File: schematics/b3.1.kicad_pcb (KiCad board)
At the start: 2 copper layers, 69.5 x 25 mm, 48 parts, among them J1 PowerInput, J2 PowerPassThru, J3 OutputPins, U1 INA128, U2 INA128, U3 INA128, U4 INA128

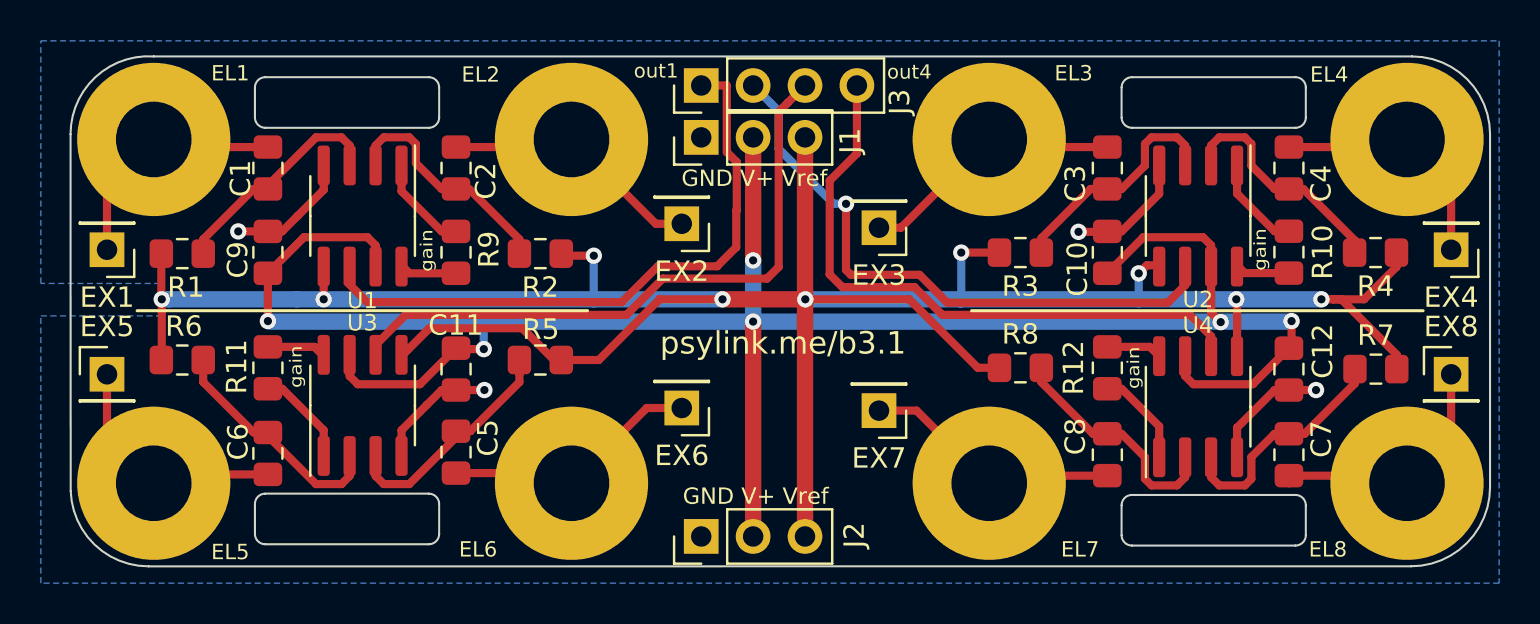
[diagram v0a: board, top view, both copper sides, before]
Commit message: On b3.1, route EX1-C1 past EL1, to allow cutting C1-EL1 if needed
same for EX2-C2 and EL2, and all the other electrodes

You may want to use external electrodes with the board, but you
currently can neither disable the built-in EL1-EL8 electrodes, nor can
you remove them since they're used for physical support.  Ideally there
should be a jumper, but there's little space.  So for the time being, if
you really want to disconnect the electrodes, you can now cut the copper
traces directly.
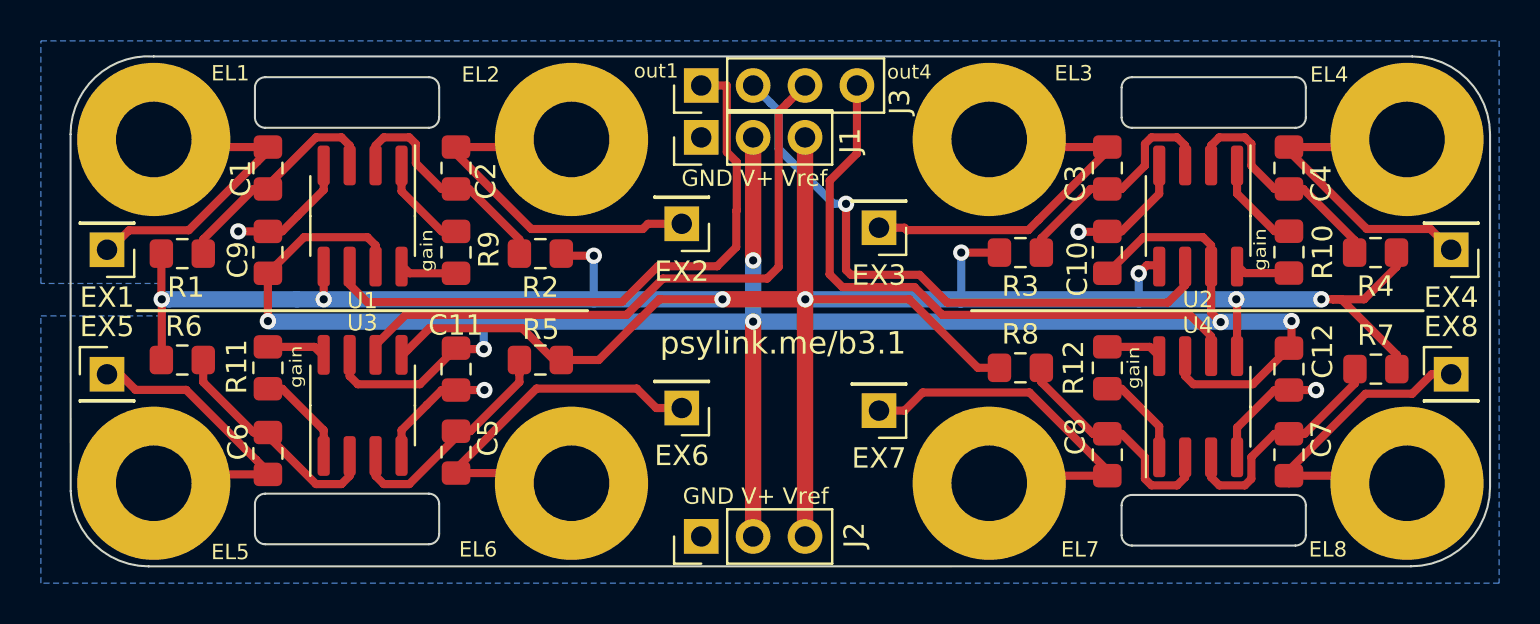
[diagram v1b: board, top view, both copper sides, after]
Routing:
- net /in1: track 12.2 -> 19.1 mm
- net /in5: track 12.0 -> 18.8 mm
- net /in7: track 12.8 -> 19.1 mm
- net /in6: track 12.8 -> 19.1 mm
- net /in2: track 12.9 -> 18.9 mm
- net /in3: track 13.1 -> 19.0 mm
- net /in4: track 12.2 -> 16.0 mm
- net /in8: track 12.2 -> 16.0 mm
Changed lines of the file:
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@@
     (thickness 1.6)
     (drawings 56)
-    (tracks 306)
+    (tracks 329)
     (zones 0)
     (modules 48)
@@
   )
   (setup
-    (last_trace_width 0.25)
+    (last_trace_width 0.4)
     (user_trace_width 0.4)
     (user_trace_width 0.5)
@@
   (segment (start 27.178 34.8615) (end 27.2415 34.798) (width 0.4) (layer F.Cu) (net 1))
   (segment (start 27.178 31.75) (end 29.464 29.464) (width 0.4) (layer F.Cu) (net 1))
-  (segment (start 27.178 34.8615) (end 27.178 31.75) (width 0.4) (layer F.Cu) (net 1))
+  (segment (start 34.544 30.5435) (end 35.179 29.9085) (width 0.4) (layer F.Cu) (net 1))
+  (segment (start 31.1785 33.909) (end 34.544 30.5435) (width 0.4) (layer F.Cu) (net 1))
+  (segment (start 28.2575 33.909) (end 31.1785 33.909) (width 0.4) (layer F.Cu) (net 1))
+  (segment (start 27.305 34.8615) (end 28.2575 33.909) (width 0.4) (layer F.Cu) (net 1))
+  (segment (start 27.178 34.8615) (end 27.305 34.8615) (width 0.4) (layer F.Cu) (net 1))
   (segment (start 39.0525 29.7605) (end 39.0525 30.7355) (width 0.4) (layer F.Cu) (net 2))
   (segment (start 38.65249 29.36049) (end 39.0525 29.7605) (width 0.4) (layer F.Cu) (net 2))
@@
   (segment (start 49.539 29.836) (end 49.911 29.464) (width 0.4) (layer F.Cu) (net 4))
   (segment (start 44.2595 29.836) (end 49.539 29.836) (width 0.4) (layer F.Cu) (net 4))
-  (segment (start 54.0385 33.5915) (end 49.911 29.464) (width 0.4) (layer F.Cu) (net 4))
-  (segment (start 55.3085 33.5915) (end 54.0385 33.5915) (width 0.4) (layer F.Cu) (net 4))
+  (segment (start 55.3085 33.5915) (end 53.6575 33.5915) (width 0.4) (layer F.Cu) (net 4))
+  (segment (start 53.6575 33.5915) (end 53.4035 33.8455) (width 0.4) (layer F.Cu) (net 4))
+  (segment (start 53.4035 33.8455) (end 47.9425 33.8455) (width 0.4) (layer F.Cu) (net 4))
+  (segment (start 44.069 29.972) (end 44.069 29.845) (width 0.4) (layer F.Cu) (net 4))
+  (segment (start 47.9425 33.8455) (end 44.069 29.972) (width 0.4) (layer F.Cu) (net 4))
   (segment (start 75.4365 31.886) (end 76.1365 31.886) (width 0.4) (layer F.Cu) (net 5))
   (segment (start 75.3222 31.886) (end 75.4365 31.886) (width 0.4) (layer F.Cu) (net 5))
@@
   (segment (start 70.73 29.836) (end 70.358 29.464) (width 0.4) (layer F.Cu) (net 6))
   (segment (start 76.1365 29.836) (end 70.73 29.836) (width 0.4) (layer F.Cu) (net 6))
-  (segment (start 66.04 33.782) (end 64.9605 33.782) (width 0.4) (layer F.Cu) (net 6))
-  (segment (start 70.358 29.464) (end 66.04 33.782) (width 0.4) (layer F.Cu) (net 6))
+  (segment (start 66.2105 33.782) (end 66.3375 33.909) (width 0.4) (layer F.Cu) (net 6))
+  (segment (start 64.9605 33.782) (end 66.2105 33.782) (width 0.4) (layer F.Cu) (net 6))
+  (segment (start 66.34531 33.90119) (end 72.27081 33.90119) (width 0.4) (layer F.Cu) (net 6))
+  (segment (start 66.3375 33.909) (end 66.34531 33.90119) (width 0.4) (layer F.Cu) (net 6))
+  (segment (start 72.771 33.401) (end 76.327 29.845) (width 0.4) (layer F.Cu) (net 6))
+  (segment (start 72.27081 33.90119) (end 72.771 33.401) (width 0.4) (layer F.Cu) (net 6))
   (segment (start 88.2396 34.3991) (end 88.2396 35.0012) (width 0.4) (layer F.Cu) (net 7))
   (segment (start 85.7265 31.886) (end 88.2396 34.3991) (width 0.4) (layer F.Cu) (net 7))
@@
   (segment (start 90.433 29.836) (end 90.805 29.464) (width 0.4) (layer F.Cu) (net 8))
   (segment (start 85.0265 29.836) (end 90.433 29.836) (width 0.4) (layer F.Cu) (net 8))
-  (segment (start 92.964 31.623) (end 90.805 29.464) (width 0.4) (layer F.Cu) (net 8))
-  (segment (start 92.964 34.8615) (end 92.964 31.623) (width 0.4) (layer F.Cu) (net 8))
+  (segment (start 92.964 34.8615) (end 91.948 33.8455) (width 0.4) (layer F.Cu) (net 8))
+  (segment (start 91.948 33.8455) (end 88.8365 33.8455) (width 0.4) (layer F.Cu) (net 8))
+  (segment (start 88.8365 33.8455) (end 84.8995 29.9085) (width 0.4) (layer F.Cu) (net 8))
   (segment (start 47.362 40.959) (end 47.362 40.259) (width 0.4) (layer F.Cu) (net 9))
   (segment (start 47.362 41.34) (end 47.362 40.959) (width 0.4) (layer F.Cu) (net 9))
@@
   (segment (start 35.052 45.856) (end 29.8995 45.856) (width 0.4) (layer F.Cu) (net 10))
   (segment (start 27.178 44.0055) (end 29.464 46.2915) (width 0.4) (layer F.Cu) (net 10))
-  (segment (start 27.178 40.9575) (end 27.178 44.0055) (width 0.4) (layer F.Cu) (net 10))
+  (segment (start 28.575 41.7195) (end 31.0515 41.7195) (width 0.4) (layer F.Cu) (net 10))
+  (segment (start 27.813 40.9575) (end 28.575 41.7195) (width 0.4) (layer F.Cu) (net 10))
+  (segment (start 31.0515 41.7195) (end 34.4805 45.1485) (width 0.4) (layer F.Cu) (net 10))
+  (segment (start 27.178 40.9575) (end 27.813 40.9575) (width 0.4) (layer F.Cu) (net 10))
+  (segment (start 34.4805 45.1485) (end 35.052 45.72) (width 0.4) (layer F.Cu) (net 10))
   (segment (start 49.412 45.7925) (end 49.911 46.2915) (width 0.4) (layer F.Cu) (net 11))
   (segment (start 44.2595 45.7925) (end 49.412 45.7925) (width 0.4) (layer F.Cu) (net 11))
-  (segment (start 53.594 42.6085) (end 49.911 46.2915) (width 0.4) (layer F.Cu) (net 11))
-  (segment (start 55.3085 42.6085) (end 53.594 42.6085) (width 0.4) (layer F.Cu) (net 11))
+  (segment (start 54.0585 42.6085) (end 53.106 41.656) (width 0.4) (layer F.Cu) (net 11))
+  (segment (start 55.3085 42.6085) (end 54.0585 42.6085) (width 0.4) (layer F.Cu) (net 11))
+  (segment (start 53.106 41.656) (end 48.1965 41.656) (width 0.4) (layer F.Cu) (net 11))
+  (segment (start 48.1965 41.656) (end 44.1325 45.72) (width 0.4) (layer F.Cu) (net 11))
   (segment (start 39.0525 45.9315) (end 39.0525 44.9565) (width 0.4) (layer F.Cu) (net 12))
   (segment (start 38.65249 46.33151) (end 39.0525 45.9315) (width 0.4) (layer F.Cu) (net 12))
@@
   (segment (start 70.73 45.9195) (end 70.358 46.2915) (width 0.4) (layer F.Cu) (net 14))
   (segment (start 76.1365 45.9195) (end 70.73 45.9195) (width 0.4) (layer F.Cu) (net 14))
-  (segment (start 66.802 42.7355) (end 70.358 46.2915) (width 0.4) (layer F.Cu) (net 14))
-  (segment (start 64.9605 42.7355) (end 66.802 42.7355) (width 0.4) (layer F.Cu) (net 14))
+  (segment (start 66.2105 42.7355) (end 67.0995 41.8465) (width 0.4) (layer F.Cu) (net 14))
+  (segment (start 64.9605 42.7355) (end 66.2105 42.7355) (width 0.4) (layer F.Cu) (net 14))
+  (segment (start 72.3265 41.8465) (end 76.2 45.72) (width 0.4) (layer F.Cu) (net 14))
+  (segment (start 67.0995 41.8465) (end 72.3265 41.8465) (width 0.4) (layer F.Cu) (net 14))
   (segment (start 72.907 41.34) (end 72.907 40.64) (width 0.4) (layer F.Cu) (net 15))
   (segment (start 75.4365 43.8695) (end 72.907 41.34) (width 0.4) (layer F.Cu) (net 15))
@@
   (segment (start 90.433 45.9195) (end 90.805 46.2915) (width 0.4) (layer F.Cu) (net 16))
   (segment (start 85.0265 45.9195) (end 90.433 45.9195) (width 0.4) (layer F.Cu) (net 16))
-  (segment (start 92.964 44.1325) (end 90.805 46.2915) (width 0.4) (layer F.Cu) (net 16))
-  (segment (start 92.964 40.9575) (end 92.964 44.1325) (width 0.4) (layer F.Cu) (net 16))
+  (segment (start 84.963 45.72) (end 84.963 45.7835) (width 0.4) (layer F.Cu) (net 16))
+  (segment (start 88.773 41.91) (end 84.963 45.72) (width 0.4) (layer F.Cu) (net 16))
+  (segment (start 91.059 41.91) (end 88.773 41.91) (width 0.4) (layer F.Cu) (net 16))
+  (segment (start 92.0115 40.9575) (end 91.059 41.91) (width 0.4) (layer F.Cu) (net 16))
+  (segment (start 92.964 40.9575) (end 92.0115 40.9575) (width 0.4) (layer F.Cu) (net 16))
   (segment (start 41.5925 44.045) (end 41.5925 45.02) (width 0.4) (layer F.Cu) (net 17))
   (segment (start 43.5595 41.7285) (end 42.8345 42.4535) (width 0.4) (layer F.Cu) (net 17))

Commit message: On b3.1, add jumpers for electrodes, so u can quickly switch to external ones
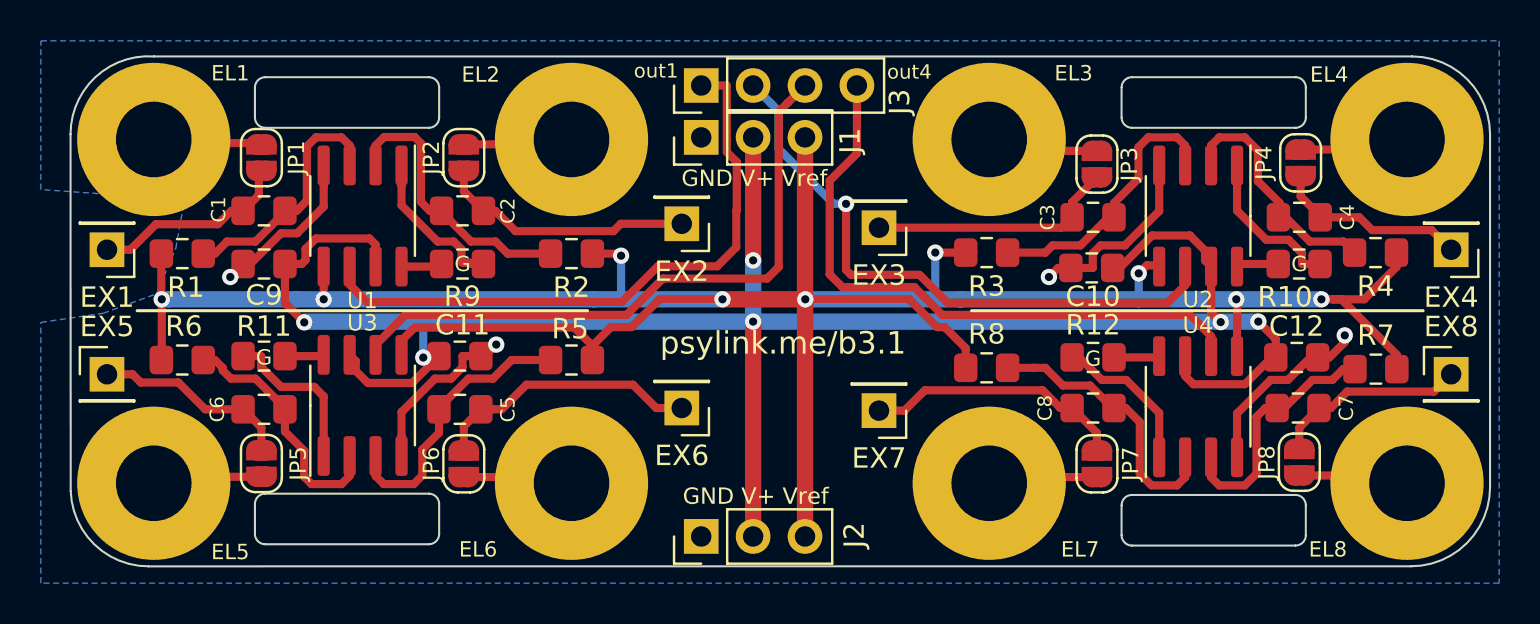
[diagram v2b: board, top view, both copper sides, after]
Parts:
- added JP1: Jumper_NO_Small, Jumper:SolderJumper-2_P1.3mm_Open_RoundedPad1.0x1.5mm, F.Cu at (34.7, 30.4)
- added JP2: Jumper_NO_Small, Jumper:SolderJumper-2_P1.3mm_Open_RoundedPad1.0x1.5mm, F.Cu at (44.6, 30.4)
- added JP3: Jumper_NO_Small, Jumper:SolderJumper-2_P1.3mm_Open_RoundedPad1.0x1.5mm, F.Cu at (75.6, 30.7)
- added JP4: Jumper_NO_Small, Jumper:SolderJumper-2_P1.3mm_Open_RoundedPad1.0x1.5mm, F.Cu at (85.6, 30.6)
- added JP5: Jumper_NO_Small, Jumper:SolderJumper-2_P1.3mm_Open_RoundedPad1.0x1.5mm, F.Cu at (34.7, 45.3)
- added JP6: Jumper_NO_Small, Jumper:SolderJumper-2_P1.3mm_Open_RoundedPad1.0x1.5mm, F.Cu at (44.6, 45.3)
- added JP7: Jumper_NO_Small, Jumper:SolderJumper-2_P1.3mm_Open_RoundedPad1.0x1.5mm, F.Cu at (75.6, 45.3)
- added JP8: Jumper_NO_Small, Jumper:SolderJumper-2_P1.3mm_Open_RoundedPad1.0x1.5mm, F.Cu at (85.5, 45.3)
- EX1, EX2, EX3, EX4, EX5, EX6, EX7, EX8: value Conn_01x01 -> ElectrodeTestPin
- moved C3 2.51 mm to (75.4, 33.3), turned to 0 degrees
- moved C4 2.47 mm to (85.5, 33.3), turned to 0 degrees
- moved C8 2.39 mm to (75.4, 42.6), turned to 180 degrees
- moved C7 2.33 mm to (85.5, 42.6), turned to 180 degrees
- moved C6 2.17 mm to (34.9, 42.7), turned to 180 degrees
- moved C2 2.12 mm to (44.6, 33.0), turned to 0 degrees
- moved C5 2.10 mm to (44.5, 42.7), turned to 180 degrees
- moved C1 2.10 mm to (34.9, 33.0), turned to 0 degrees
- moved R3 1.65 mm to (70.2, 35.0)
- moved R8 1.65 mm to (70.2, 40.6)
- moved R2 1.52 mm to (49.9, 35.1)
- moved R5 1.52 mm to (49.9, 40.3)
- moved C10 1.08 mm to (75.4, 35.8), turned to 180 degrees
- moved R12 0.86 mm to (75.4, 40.1), turned to 0 degrees
- moved R10 0.77 mm to (85.5, 35.6), turned to 180 degrees
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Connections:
- EL1 pad 1: /in1 -> Net-(EL1-Pad1)
- EL2 pad 1: /in2 -> Net-(EL2-Pad1)
- EL3 pad 1: /in3 -> Net-(EL3-Pad1)
- EL4 pad 1: /in4 -> Net-(EL4-Pad1)
- EL5 pad 1: /in5 -> Net-(EL5-Pad1)
- EL6 pad 1: /in6 -> Net-(EL6-Pad1)
- EL7 pad 1: /in7 -> Net-(EL7-Pad1)
- EL8 pad 1: /in8 -> Net-(EL8-Pad1)
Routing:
- net Earth: track 24.7 -> 35.1 mm
- net /in1: track 19.1 -> 9.87 mm
- net /in5: track 18.8 -> 9.74 mm
- net Net-(EL5-Pad1): track 0.00 -> 8.63 mm
- net Net-(EL1-Pad1): track 0.00 -> 8.45 mm
- net /in3: track 19.0 -> 12.1 mm
- net /in4: track 16.0 -> 9.50 mm
- net /in8: track 16.0 -> 9.55 mm
- net /in7: track 19.1 -> 12.8 mm
- net /in2: track 18.9 -> 12.6 mm
- net /in6: track 19.1 -> 13.2 mm
- net Net-(EL3-Pad1): track 0.00 -> 5.50 mm
- net Net-(EL8-Pad1): track 0.00 -> 5.43 mm
- net Net-(EL4-Pad1): track 0.00 -> 5.41 mm
- net Net-(EL7-Pad1): track 0.00 -> 5.40 mm
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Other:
- board text added: "G"
- board text added: "This hole in the fill area breaks the ground loop"
- board text removed: "gain"
